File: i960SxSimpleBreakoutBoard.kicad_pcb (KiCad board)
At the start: 4 copper layers, 80.1 x 66.6 mm, 26 parts, among them J1 Conn_01x07, J2 Pure Input Pins, J3 Clock, Power, and Bidirection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, J4 Conn_01x05, J5 Multiplexed Address/Data Lines, J6 Upper 16 Address Lines, U1 80960Sx

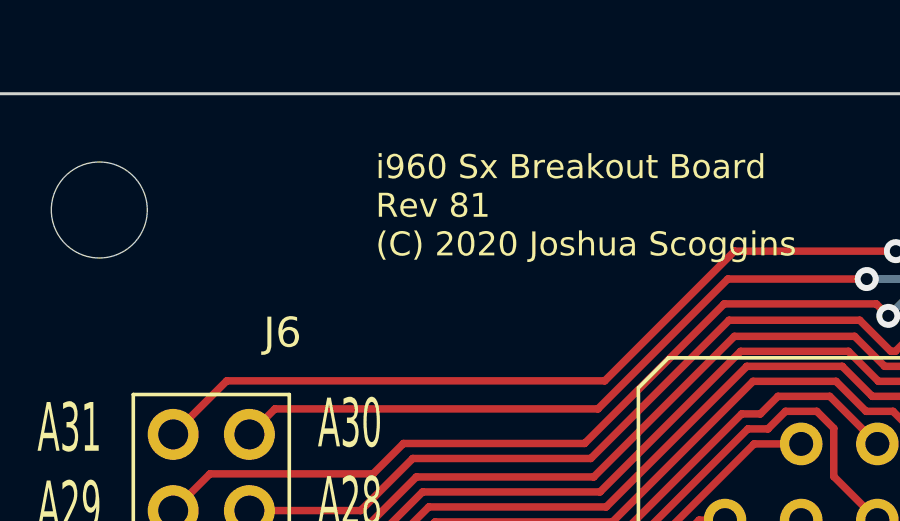
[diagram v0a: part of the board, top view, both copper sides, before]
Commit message: go with a single 1 row connector for the right side of the design
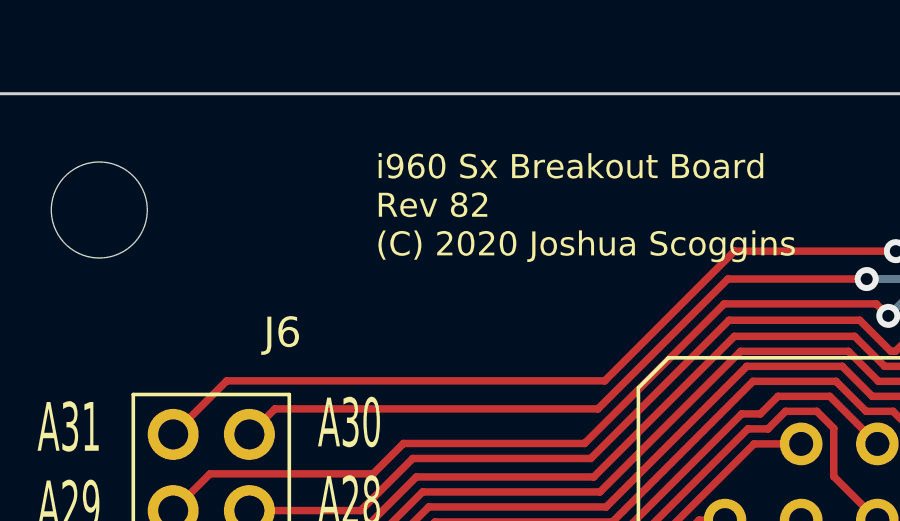
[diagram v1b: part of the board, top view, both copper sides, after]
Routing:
- removed copper zone on In1.Cu, net +5V
- removed copper zone on In2.Cu, net GND
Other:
- board text added: "i960 Sx Breakout Board Rev 82 (C) 2020 Joshua Scoggins"
- board text removed: "i960 Sx Breakout Board Rev 81 (C) 2020 Joshua Scoggins"

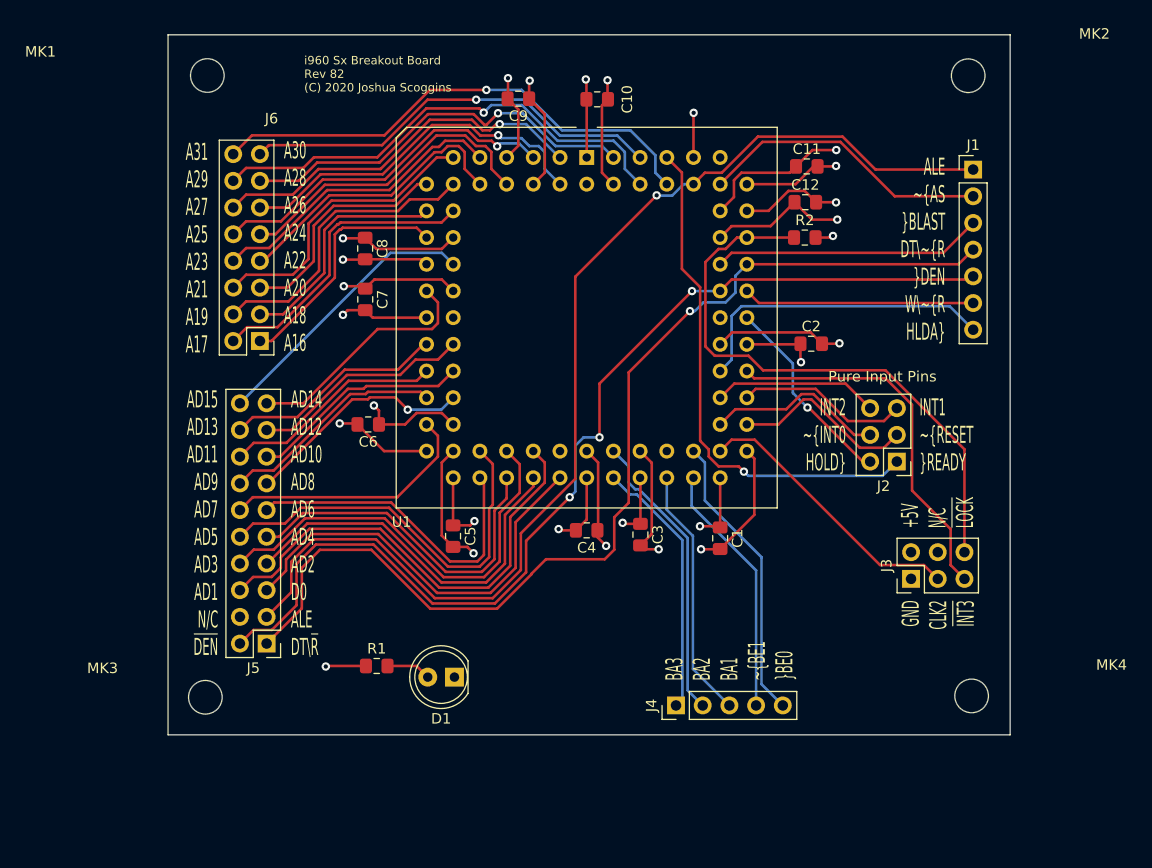
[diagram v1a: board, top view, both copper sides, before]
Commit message: Shrunk the size of the final pcb
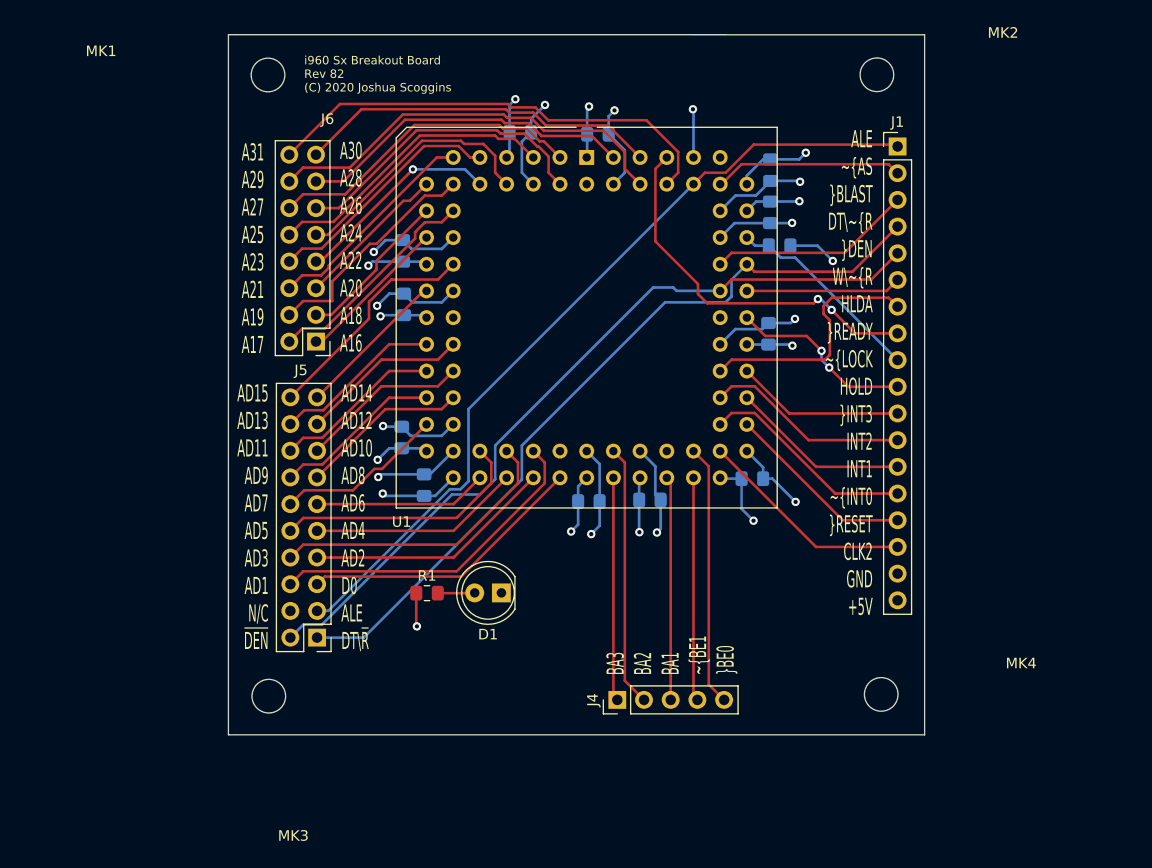
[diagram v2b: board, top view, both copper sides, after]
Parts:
- removed J2: Pure Input Pins, Connector_PinHeader_2.54mm:PinHeader_2x03_P2.54mm_Vertical
- removed J3: Clock, Power, and Bidirectional Pins, Connector_PinHeader_2.54mm:PinHeader_2x03_P2.54mm_Vertical
- C1, C10, C11, C12, C2, C3, C4, C5, C6, C7, C8, C9, R2: moved to B.Cu
- J1: value Conn_01x07 -> Conn_01x18; footprint Connector_PinHeader_2.54mm:PinHeader_1x07_P2.54mm_Vertical -> Connector_PinHeader_2.54mm:PinHeader_1x18_P2.54mm_Vertical
- moved D1 9.18 mm to (-7.08, 39.3)
- moved MK2 8.69 mm to (28.7, -10.0)
- moved MK4 8.60 mm to (29.1, 48.9)
- moved R1 8.42 mm to (-14.2, 39.3)
- moved J1 7.52 mm to (30.6, -3.20)
- moved C1 6.45 mm to (16.8, 28.4), turned to 0 degrees
- moved MK3 6.04 mm to (-29.2, 49.1)
- moved MK1 5.77 mm to (-29.3, -10.00)
- moved J4 5.61 mm to (3.95, 49.5)
- moved C5 5.58 mm to (-14.4, 29.0), turned to 90 degrees
- moved J6 5.33 mm to (-24.7, 15.4)
- moved J5 4.83 mm to (-24.6, 43.5)
- moved C2 4.17 mm to (18.3, 14.6), turned to 90 degrees
- moved C7 3.69 mm to (-16.4, 11.8)
- moved C8 3.58 mm to (-16.5, 6.73)
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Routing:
- net GND: track 124.3 -> 85.0 mm
- net /~LOCK: track 55.9 -> 19.2 mm
- net /ALE: track 107.1 -> 77.7 mm, vias 1 -> 0
- net +5V: track 120.5 -> 95.2 mm
- net /DT\~R: track 99.7 -> 74.9 mm, vias 1 -> 0
- net /~DEN: track 98.5 -> 75.1 mm, vias 3 -> 0
- net /~INT3: track 35.7 -> 16.0 mm
- net /AD6: track 31.0 -> 16.5 mm
- net /AD5: track 38.3 -> 24.5 mm
- net /AD4: track 33.7 -> 20.1 mm
- net /~READY: track 49.3 -> 36.0 mm, vias 1 -> 2
- net /AD3: track 41.2 -> 28.1 mm
- net /AD1: track 44.6 -> 31.7 mm
- net /AD2: track 36.6 -> 23.7 mm
- net /D0: track 40.2 -> 27.3 mm
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- added copper zone on In1.Cu, net +5V
- added copper zone on In2.Cu, net GND
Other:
- board size 80.1 x 66.6 mm -> 66.2 x 66.6 mm
- board text added: "ALE ~AS ~BLAST DT\~R ~DEN W\~R HLDA ~READY ~LOCK HOLD ~INT3 INT2 INT1 ~INT0 ~RESET CLK2 GND +5V"
- board text removed: "+5V N/C ~LOCK"
- board text removed: "ALE ~AS ~BLAST DT\~R ~DEN W\~R HLDA"
- board text removed: "GND CLK2 ~INT3"
- board text removed: "INT1 ~RESET ~READY"
- board text removed: "INT2 ~INT0 HOLD"

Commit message: Merge upper and lower address/data lines pin headers into a single 02x19 header layout
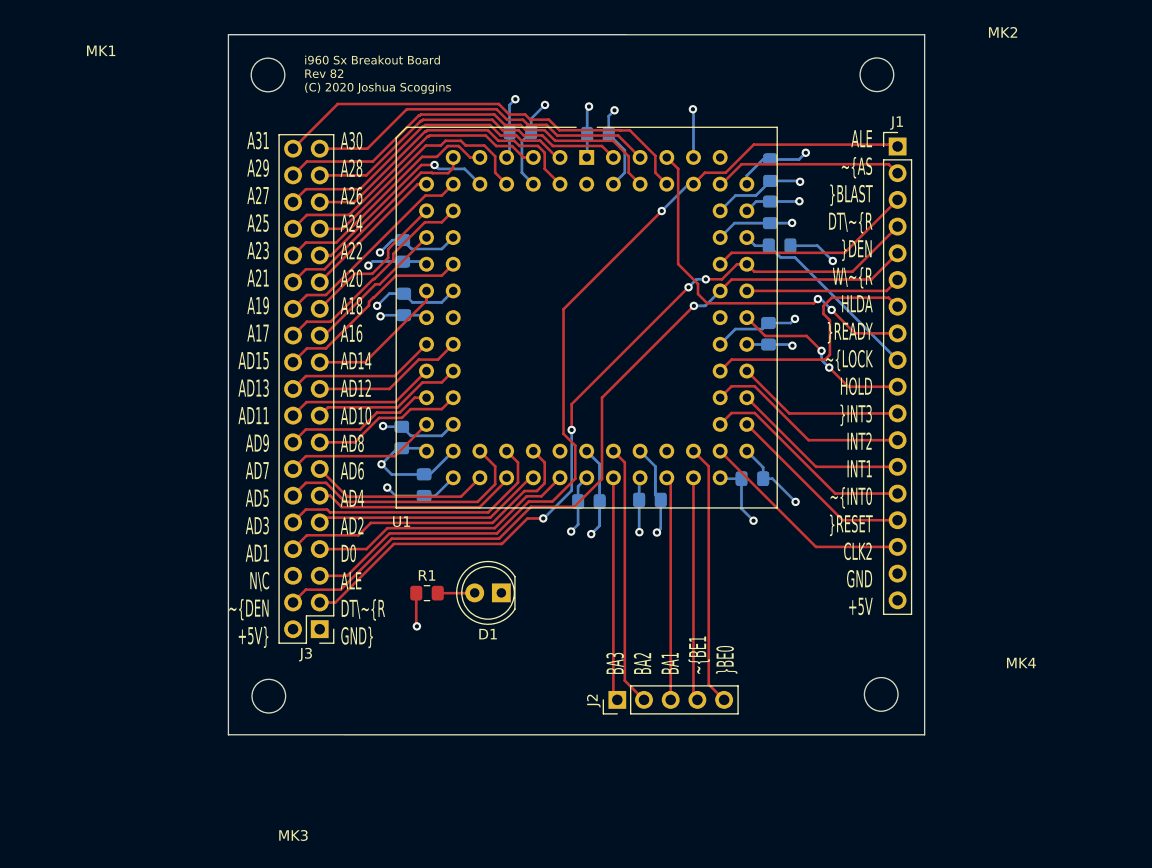
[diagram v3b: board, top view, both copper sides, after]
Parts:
- removed J5: Multiplexed Address/Data Lines, Connector_PinHeader_2.54mm:PinHeader_2x10_P2.54mm_Vertical
- removed J6: Upper 16 Address Lines, Connector_PinHeader_2.54mm:PinHeader_2x08_P2.54mm_Vertical
- added J3: Conn_02x19_Counter_Clockwise, Connector_PinHeader_2.54mm:PinHeader_2x19_P2.54mm_Vertical, F.Cu at (-24.4, 42.7)
- renumbered J4 to J2
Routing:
- net /ALE: track 77.7 -> 83.1 mm, vias 0 -> 1
- net /A31: track 44.4 -> 41.4 mm
- net /AD15: track 21.7 -> 19.3 mm
- net /A19: track 21.8 -> 20.2 mm
- net /AD9: track 16.1 -> 14.5 mm
- net /AD10: track 16.1 -> 14.5 mm
- net /AD8: track 16.1 -> 14.5 mm
- net /AD1: track 31.7 -> 30.1 mm
- net /D0: track 27.3 -> 25.7 mm
- net /AD7: track 16.1 -> 14.5 mm
- net /AD13: track 16.1 -> 14.5 mm
- net /AD12: track 16.1 -> 14.5 mm
- net /AD11: track 16.1 -> 14.5 mm
- net /AD2: track 23.7 -> 22.1 mm
- net /AD3: track 28.1 -> 26.6 mm
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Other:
- board text added: "A30 A28 A26 A24 A22 A20 A18 A16 AD14 AD12 AD10 AD8 AD6 AD4 AD2 D0 ALE DT\~R GND"
- board text added: "A31 A29 A27 A25 A23 A21 A19 A17 AD15 AD13 AD11 AD9 AD7 AD5 AD3 AD1 N\C ~DEN +5V"
- board text removed: "A30 A28 A26 A24 A22 A20 A18 A16"
- board text removed: "A31 A29 A27 A25 A23 A21 A19 A17"
- board text removed: "AD14 AD12 AD10 AD8 AD6 AD4 AD2 D0 ALE DT\~R"
- board text removed: "AD15 AD13 AD11 AD9 AD7 AD5 AD3 AD1 N/C ~DEN"

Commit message: Shave off some dimensions
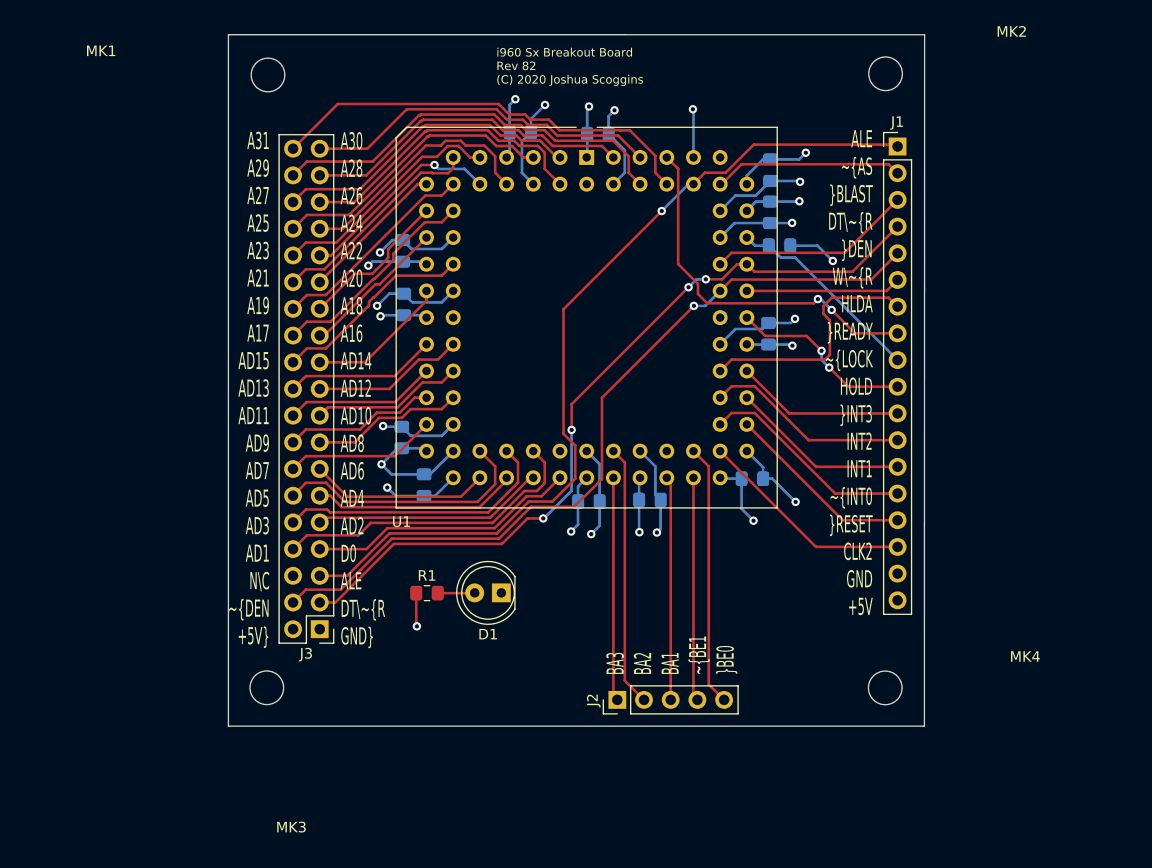
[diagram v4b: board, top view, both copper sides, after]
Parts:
- moved MK2 0.83 mm to (29.5, -10.1)
- moved MK3 0.82 mm to (-29.4, 48.3)
- moved MK4 0.73 mm to (29.4, 48.3)
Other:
- board size 66.2 x 66.6 mm -> 66.2 x 65.8 mm
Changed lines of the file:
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@@
   )
   (module MountingHole:MountingHole_3.2mm_M3 (layer Front)
-    (at 29.06268 48.93818)
+    (at 29.44622 48.31588)
     (descr "Mounting Hole 3.2mm, no annular, M3")
     (tags "mounting hole 3.2mm no annular m3")
@@
   )
   (module MountingHole:MountingHole_3.2mm_M3 (layer Front)
-    (at -29.20746 49.10582)
+    (at -29.39796 48.30572)
     (descr "Mounting Hole 3.2mm, no annular, M3")
     (tags "mounting hole 3.2mm no annular m3")
@@
   )
   (module MountingHole:MountingHole_3.2mm_M3 (layer Front)
-    (at 28.6512 -10.0203)
+    (at 29.4767 -10.11428)
     (descr "Mounting Hole 3.2mm, no annular, M3")
     (tags "mounting hole 3.2mm no annular m3")
@@
     )
   )
-  (gr_text "i960 Sx Breakout Board\nRev 82\n(C) 2020 Joshua Scoggins" (at -25.84704 -10.09396) (layer F.SilkS)
+  (gr_text "i960 Sx Breakout Board\nRev 82\n(C) 2020 Joshua Scoggins" (at -7.565213 -10.84072) (layer F.SilkS)
     (effects (font (size 0.8 0.8) (thickness 0.1)) (justify left))
   )
-  (gr_line (start 33.19272 -13.82776) (end 33.19272 52.78374) (layer Edge.Cuts) (width 0.1))
+  (gr_line (start 33.19272 -13.82776) (end 33.16986 51.95824) (layer Edge.Cuts) (width 0.1))
   (gr_line (start -33.05048 -13.8303) (end 33.19272 -13.82776) (layer Edge.Cuts) (width 0.1))
-  (gr_line (start -33.05048 52.7812) (end -33.05048 -13.8303) (layer Edge.Cuts) (width 0.1))
-  (gr_line (start 33.19272 52.78374) (end -33.05048 52.7812) (layer Edge.Cuts) (width 0.1))
+  (gr_line (start -33.05048 51.95824) (end -33.05048 -13.8303) (layer Edge.Cuts) (width 0.1))
+  (gr_line (start 33.16986 51.95824) (end -33.05048 51.95824) (layer Edge.Cuts) (width 0.1))
   (gr_text "ALE\n~AS\n~BLAST\nDT\\~R\n~DEN\nW\\~R\nHLDA\n~READY\n~LOCK\nHOLD\n~INT3\nINT2\nINT1\n~INT0\n~RESET\nCLK2\nGND\n+5V" (at 28.26258 18.36928) (layer F.SilkS)
     (effects (font (size 1.6256 0.8) (thickness 0.1)) (justify right))
@@
   (segment (start 23.007056 6.24586) (end 24.457905 7.696709) (width 0.25) (layer Back) (net 2))
   (via (at 24.457905 7.696709) (size 0.8) (drill 0.4) (layers Front Back) (net 2))
-  (via (at -15.11554 42.46372) (size 0.8) (drill 0.4) (layers Front Back) (net 2))
-  (segment (start -15.18042 39.30396) (end -15.18042 42.39884) (width 0.25) (layer Front) (net 2))
-  (segment (start -15.18042 42.39884) (end -15.11554 42.46372) (width 0.25) (layer Front) (net 2))
   (segment (start -15.542519 11.634101) (end -12.747101 11.634101) (width 0.25) (layer Back) (net 2))
   (segment (start -12.747101 11.634101) (end -11.6609 10.5479) (width 0.25) (layer Back) (net 2))
@@
   (segment (start -17.447687 5.70854) (end -18.627399 6.888252) (width 0.25) (layer Back) (net 2))
   (via (at -18.627399 6.888252) (size 0.8) (drill 0.4) (layers Front Back) (net 2) (status 40000))
+  (via (at -15.11554 42.46372) (size 0.8) (drill 0.4) (layers Front Back) (net 2) (status 1000000))
+  (segment (start -15.18042 39.30396) (end -15.18042 42.39884) (width 0.25) (layer Front) (net 2) (status 1000000))
+  (segment (start -15.18042 42.39884) (end -15.11554 42.46372) (width 0.25) (layer Front) (net 2) (status 1000000))
   (segment (start 13.881398 0.3879) (end 15.774617 -1.505319) (width 0.25) (layer Front) (net 3))
   (segment (start 29.769701 -1.505319) (end 30.6197 -0.65532) (width 0.25) (layer Front) (net 3))
@@
   (segment (start 25.582681 6.921699) (end 30.6197 1.88468) (width 0.25) (layer Front) (net 9))
   (segment (start 14.825301 6.921699) (end 25.582681 6.921699) (width 0.25) (layer Front) (net 9))
-  (segment (start 3.5791 49.08574) (end 3.95224 49.45888) (width 0.25) (layer Front) (net 10))
-  (segment (start 3.5791 28.3279) (end 3.5791 49.08574) (width 0.25) (layer Front) (net 10))
-  (segment (start 4.665301 47.631941) (end 4.665301 26.874101) (width 0.25) (layer Front) (net 11))
-  (segment (start 4.665301 26.874101) (end 3.5791 25.7879) (width 0.25) (layer Front) (net 11))
-  (segment (start 6.49224 49.45888) (end 4.665301 47.631941) (width 0.25) (layer Front) (net 11))
-  (segment (start 9.03224 28.70104) (end 8.6591 28.3279) (width 0.25) (layer Front) (net 12))
-  (segment (start 9.03224 49.45888) (end 9.03224 28.70104) (width 0.25) (layer Front) (net 12))
+  (segment (start 3.5791 28.3279) (end 3.5791 49.08574) (width 0.25) (layer Front) (net 10) (status 1000000))
+  (segment (start 3.5791 49.08574) (end 3.95224 49.45888) (width 0.25) (layer Front) (net 10) (status 1000000))
+  (segment (start 6.49224 49.45888) (end 4.665301 47.631941) (width 0.25) (layer Front) (net 11) (status 1000000))
+  (segment (start 4.665301 47.631941) (end 4.665301 26.874101) (width 0.25) (layer Front) (net 11) (status 1000000))
+  (segment (start 4.665301 26.874101) (end 3.5791 25.7879) (width 0.25) (layer Front) (net 11) (status 1000000))
+  (segment (start 9.03224 49.45888) (end 9.03224 28.70104) (width 0.25) (layer Front) (net 12) (status 1000000))
+  (segment (start 9.03224 28.70104) (end 8.6591 28.3279) (width 0.25) (layer Front) (net 12) (status 1000000))
   (segment (start 14.825301 19.621699) (end 17.025777 19.621699) (width 0.25) (layer Front) (net 13))
   (segment (start 22.148758 24.74468) (end 30.6197 24.74468) (width 0.25) (layer Front) (net 13))
@@
   (segment (start -19.060257 9.915721) (end -18.648721 9.915721) (width 0.25) (layer Front) (net 37))
   (segment (start -23.937496 14.79296) (end -19.060257 9.915721) (width 0.25) (layer Front) (net 37))
-  (segment (start 11.1991 49.08574) (end 11.57224 49.45888) (width 0.25) (layer Front) (net 38))
-  (segment (start 11.1991 28.3279) (end 11.1991 49.08574) (width 0.25) (layer Front) (net 38))
+  (segment (start 11.1991 49.08574) (end 11.57224 49.45888) (width 0.25) (layer Front) (net 38) (status 1000000))
+  (segment (start 11.1991 28.3279) (end 11.1991 49.08574) (width 0.25) (layer Front) (net 38) (status 1000000))
   (segment (start -3.260408 30.087408) (end -1.5009 28.3279) (width 0.25) (layer Front) (net 39))
   (segment (start -17.923813 33.120167) (end -7.710473 33.120167) (width 0.25) (layer Front) (net 39))
@@
   (segment (start -7.710473 33.120167) (end -4.677714 30.087408) (width 0.25) (layer Front) (net 39))
   (segment (start -4.677714 30.087408) (end -3.260408 30.087408) (width 0.25) (layer Front) (net 39))
-  (segment (start 12.652899 27.241699) (end 11.1991 25.7879) (width 0.25) (layer Front) (net 40))
-  (segment (start 12.652899 47.999539) (end 12.652899 27.241699) (width 0.25) (layer Front) (net 40))
-  (segment (start 14.11224 49.45888) (end 12.652899 47.999539) (width 0.25) (layer Front) (net 40))
+  (segment (start 14.11224 49.45888) (end 12.652899 47.999539) (width 0.25) (layer Front) (net 40) (status 1000000))
+  (segment (start 12.652899 27.241699) (end 11.1991 25.7879) (width 0.25) (layer Front) (net 40) (status 1000000))
+  (segment (start 12.652899 47.999539) (end 12.652899 27.241699) (width 0.25) (layer Front) (net 40) (status 1000000))
   (segment (start -4.33245 28.3279) (end -4.0409 28.3279) (width 0.25) (layer Front) (net 41))
   (segment (start -23.908325 32.120145) (end -8.124695 32.120145) (width 0.25) (layer Front) (net 41))
@@
   (segment (start -26.90114 17.33296) (end -25.586141 16.017961) (width 0.25) (layer Front) (net 55))
   (segment (start -19.273589 11.189574) (end -19.215451 11.189573) (width 0.25) (layer Front) (net 55))
-  (segment (start -9.64184 39.30396) (end -9.61644 39.27856) (width 0.25) (layer Front) (net 56))
-  (segment (start -13.13042 39.30396) (end -9.64184 39.30396) (width 0.25) (layer Front) (net 56))
+  (segment (start -9.64184 39.30396) (end -9.61644 39.27856) (width 0.25) (layer Front) (net 56) (status 1000000))
+  (segment (start -13.13042 39.30396) (end -9.64184 39.30396) (width 0.25) (layer Front) (net 56) (status 1000000))
   (zone (net 0) (net_name "") (layers Front In1.Cu In2.Cu Back) (hatch edge 0.508)
     (connect_pads (clearance 0.508))
@@
     (polygon
       (pts
-        (xy 38.1254 55.87746) (xy -36.22802 55.87746) (xy -36.22802 -17.70634) (xy 38.1254 -17.70634)
+        (xy 38.94328 56.15432) (xy -35.8775 56.15432) (xy -35.8775 -16.42872) (xy 38.94328 -16.42872)
       )
     )
@@
     (polygon
       (pts
-        (xy 36.7411 54.55158) (xy -35.15868 54.55158) (xy -35.15868 -16.90116) (xy 36.7411 -16.90116)
+        (xy 35.50158 54.56428) (xy -34.33826 54.56428) (xy -34.33826 -15.3162) (xy 35.50158 -15.3162)
       )
     )
